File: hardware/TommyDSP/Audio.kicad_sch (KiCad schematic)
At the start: 39 parts, among them U301 ES8388/WM8988

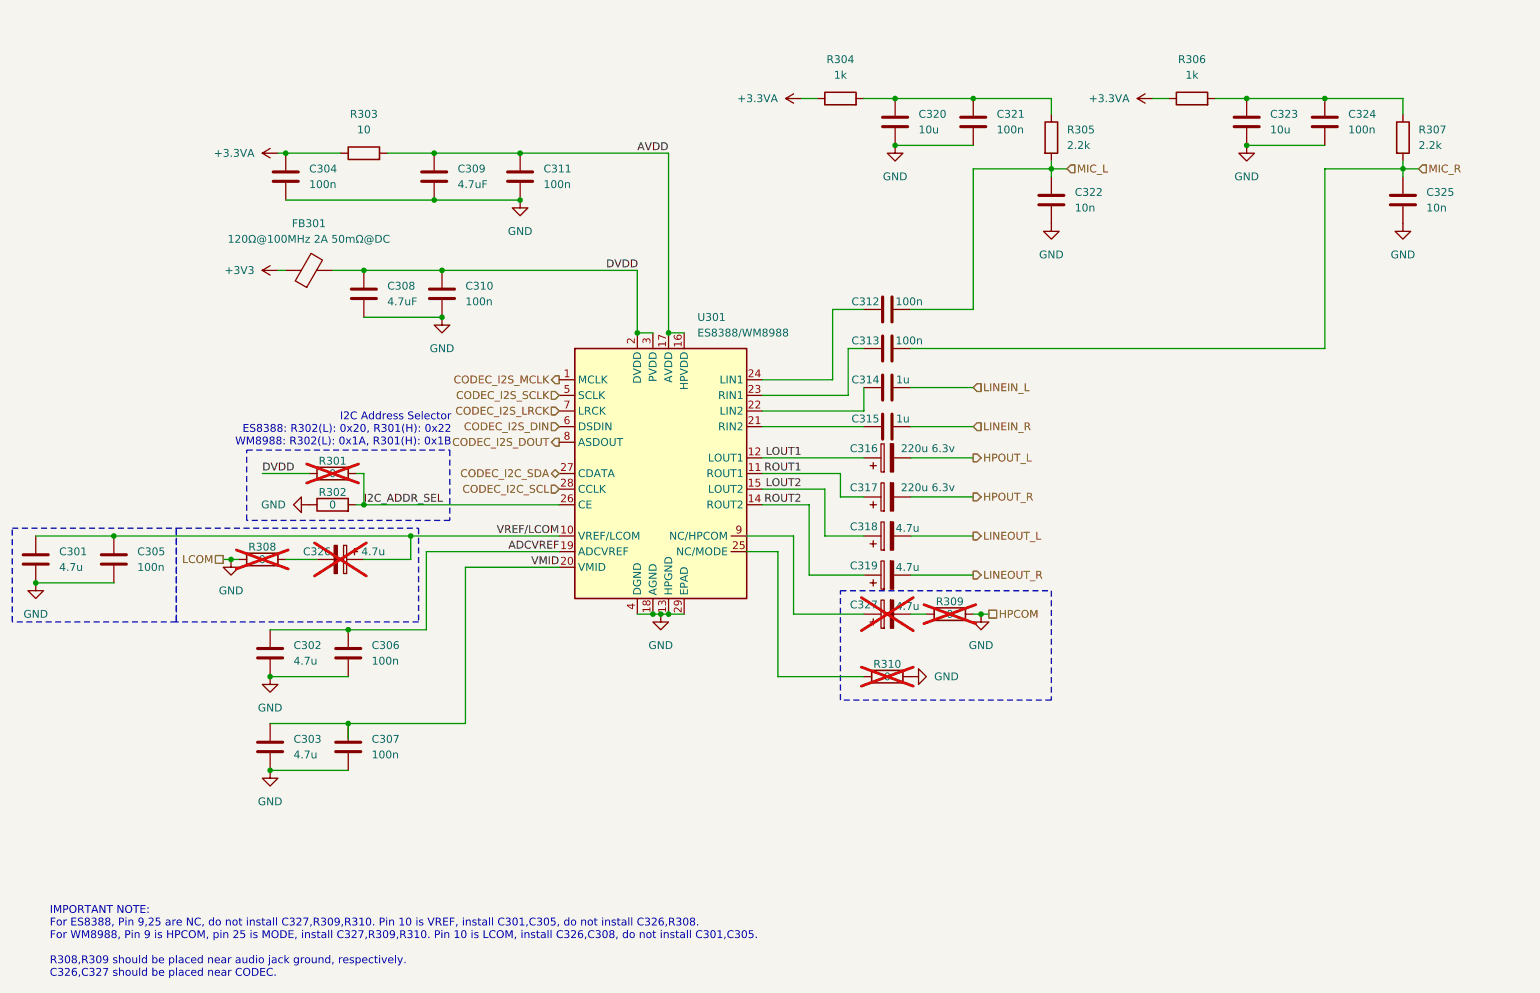
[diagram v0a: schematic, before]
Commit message: hardware: add PAM8406 audio amplifier board
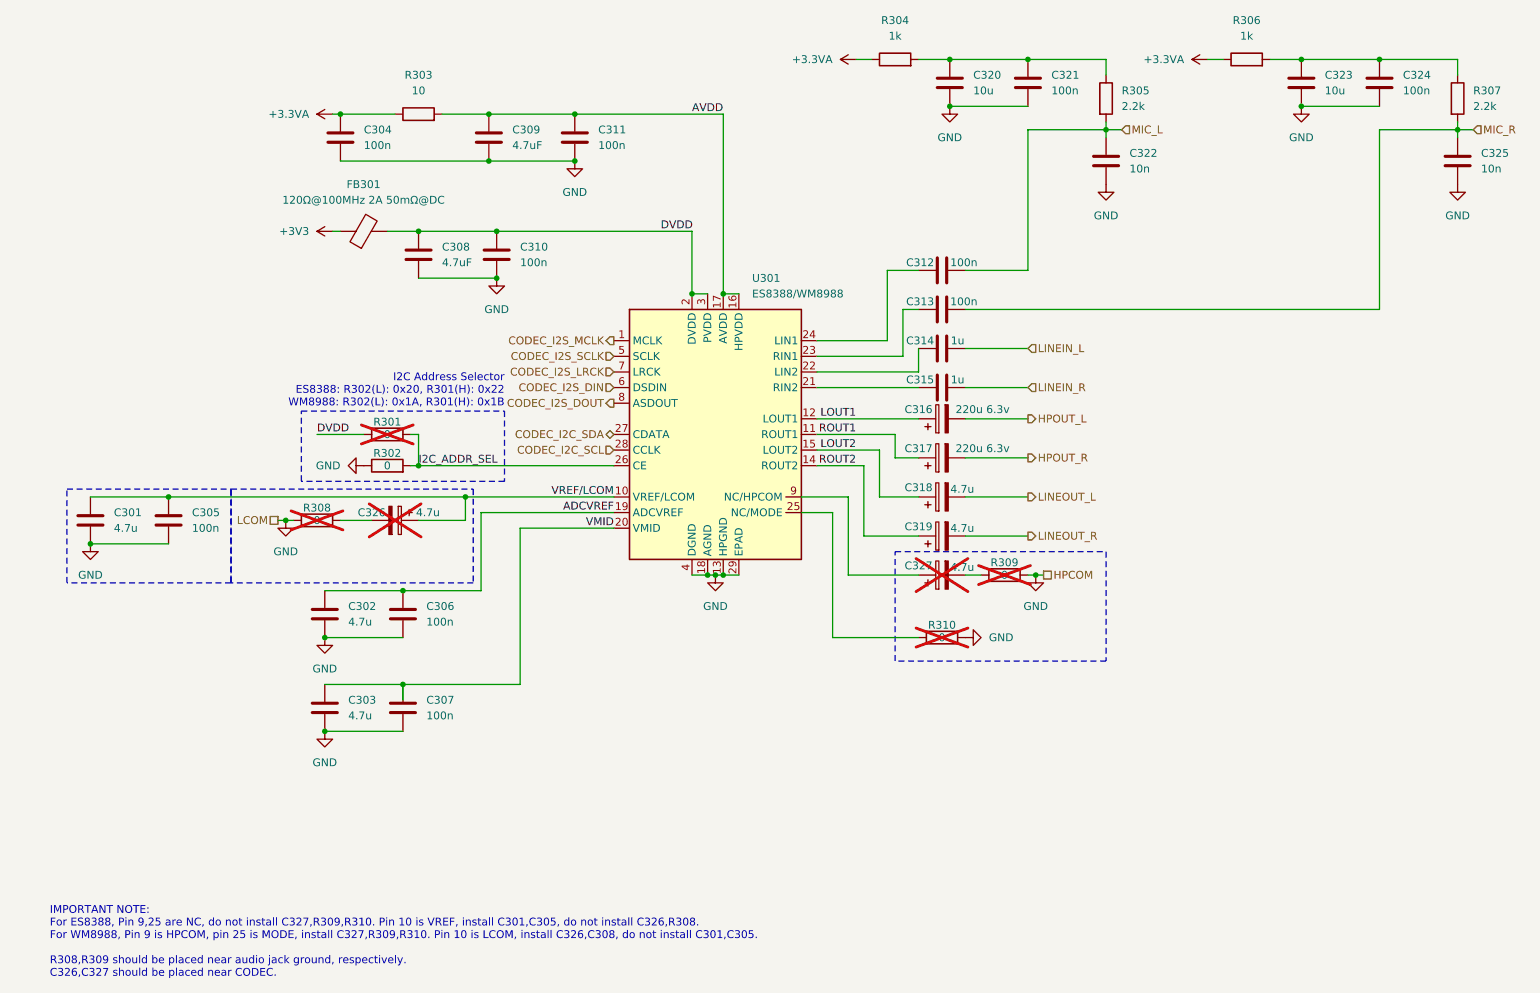
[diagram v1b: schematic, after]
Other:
- moved on the sheet: C301, C302, C303, C304, C305, C306, C307, C308, C309, C310, C311, C312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

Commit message: bump to KiCad V10, add logo
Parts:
- C326, C327, R301, R308, R309, R310: now left out of the parts list
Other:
- title: Audio CODEC -> TommyDSP
